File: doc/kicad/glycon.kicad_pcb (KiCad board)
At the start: 2 copper layers, 200 x 100 mm, 74 parts, among them IC2 CTC-DIP-28, J1 Arduino/system bus header, J2 PMOD USBUART conn, J3 Conn_02x24_Odd_Even, J4 Conn_01x02, J5 USB_B, Q1 IRF9540N, Q2 IRF9540N, SW1 SW_Push, SW2 SW_Push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

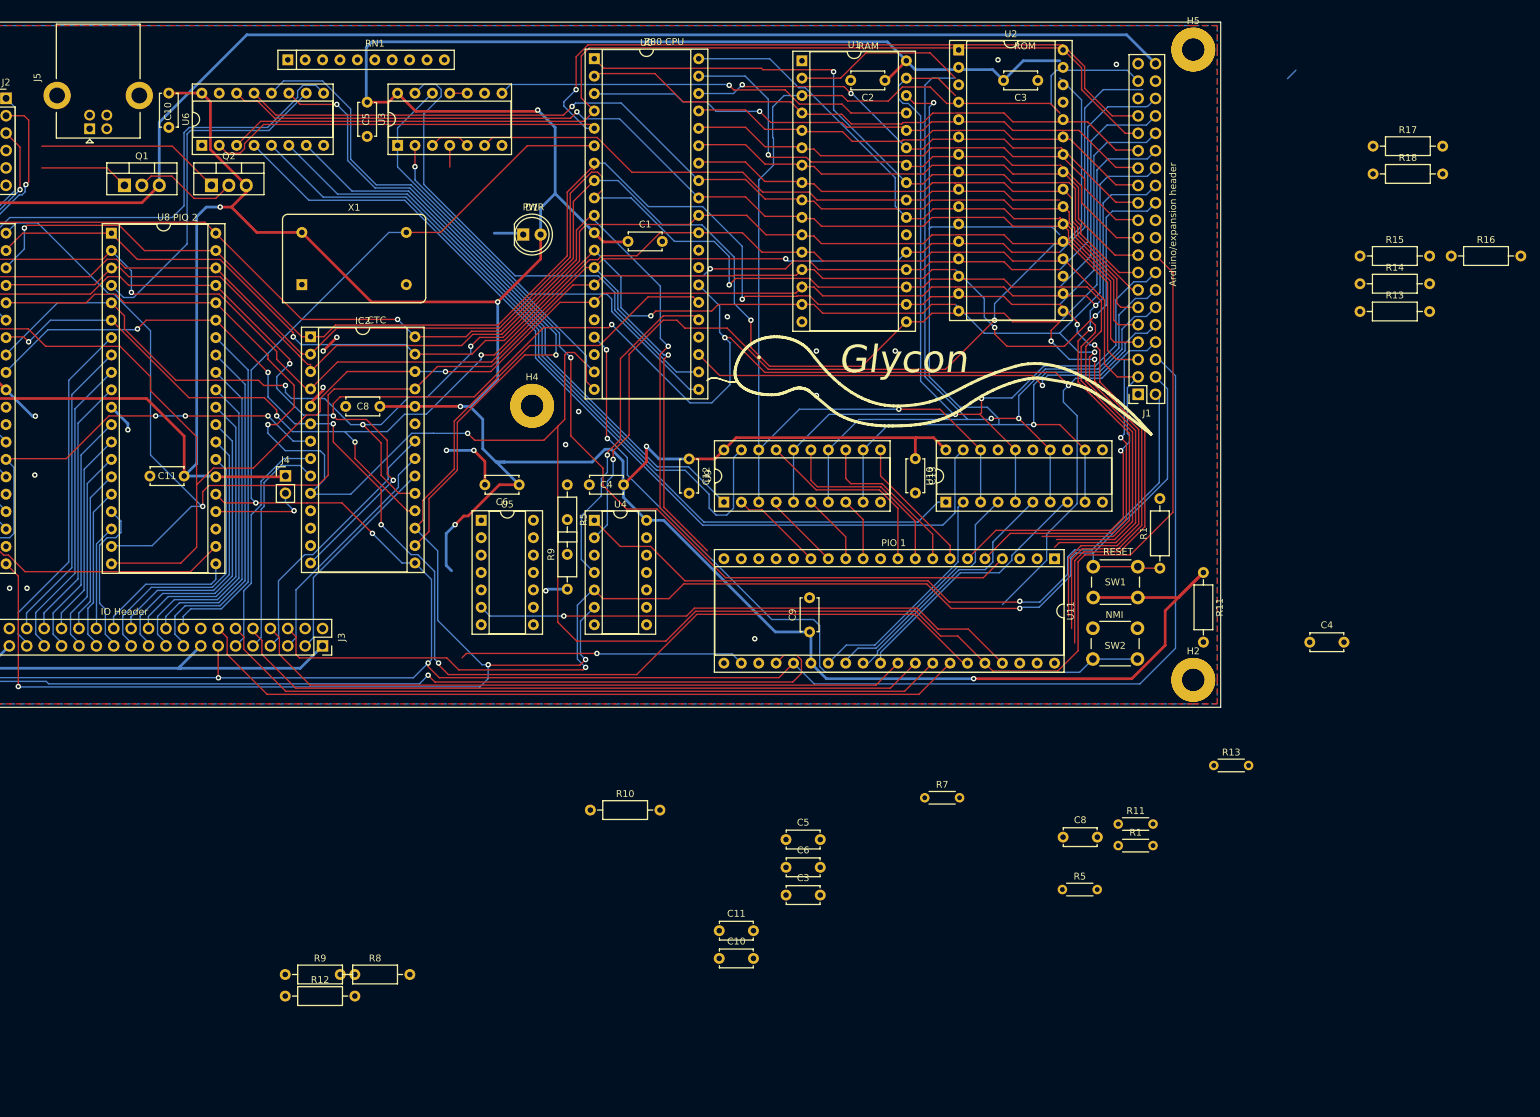
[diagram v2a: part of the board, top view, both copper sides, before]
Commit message: add resistor pack to pcb
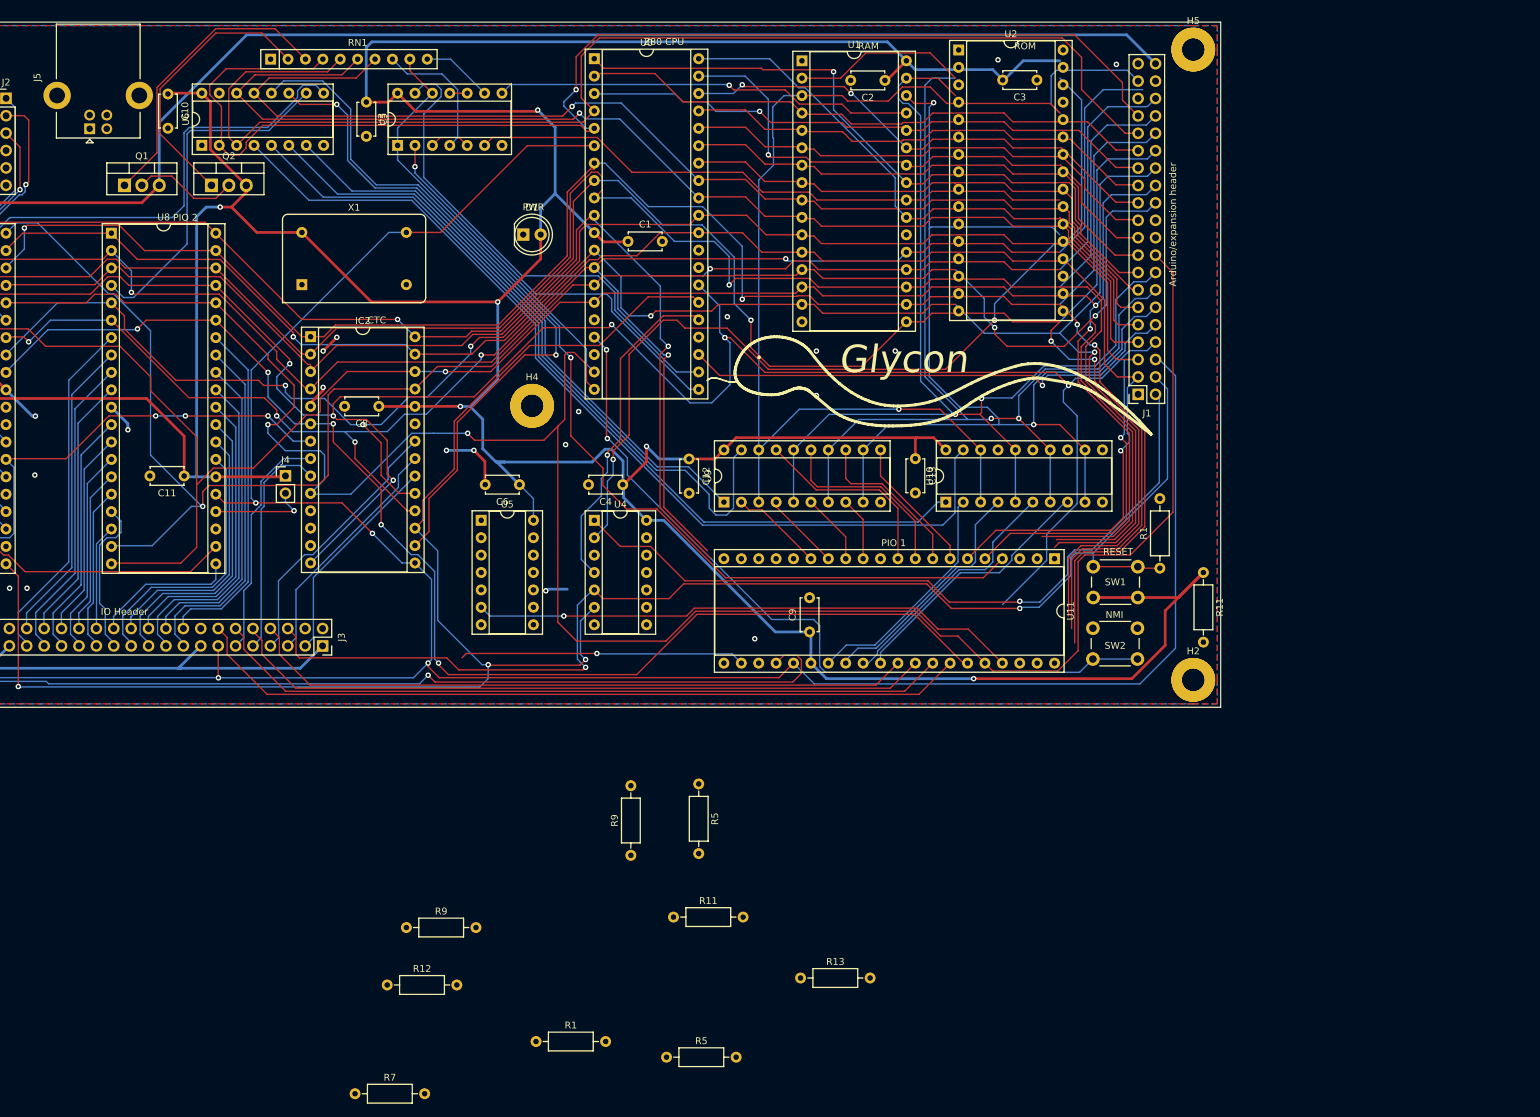
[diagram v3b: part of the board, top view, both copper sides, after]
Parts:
- removed the C10 at (70.0, 30.4)
- removed the C11 at (72.2, 86.2)
- removed the C3 at (196.8, 28.5)
- removed the C4 at (136.3, 87.5)
- removed the C5 at (98.9, 31.7)
- removed the C6 at (121.1, 87.5)
- removed the C8 at (100.8, 76.1)
- removed the C8 at (200.5, 138.9)
- removed R10, R14, R15, R16, R17, R18, R8: 10K, Resistor_THT:R_Axial_DIN0207_L6.3mm_D2.5mm_P10.16mm_Horizontal
- removed the R13 at (243.8, 62.2)
- removed the R13 at (222.5, 128.5)
- added C8: 100nF, Capacitor_THT:C_Disc_D4.7mm_W2.5mm_P5.00mm, F.Cu at (100.6, 76.1)
- added R13: 10K, Resistor_THT:R_Axial_DIN0207_L6.3mm_D2.5mm_P10.16mm_Horizontal, F.Cu at (162.2, 159.5)
- R1, R11, R5, R7: footprint Resistor_THT:R_Axial_DIN0204_L3.6mm_D1.6mm_P5.08mm_Horizontal -> Resistor_THT:R_Axial_DIN0207_L6.3mm_D2.5mm_P10.16mm_Horizontal
- moved C10 149.6 mm to (69.8, 30.5), turned to -90 degrees
- moved C3 124.5 mm to (196.7, 28.4), turned to 180 degrees
- moved C5 123.9 mm to (98.8, 31.7), turned to -90 degrees
- moved C4 102.9 mm to (136.2, 87.5), turned to 180 degrees
- moved C11 102.5 mm to (72.2, 86.2), turned to 180 degrees
- moved R7 93.7 mm to (97.2, 176.4)
- moved R1 89.7 mm to (123.6, 168.8)
- moved C6 68.1 mm to (121.2, 87.5), turned to 180 degrees
- moved R11 66.3 mm to (143.6, 150.6)
- moved R5 62.7 mm to (142.6, 171.1)
- moved R5 47.7 mm to (147.3, 131.2)
- moved R9 39.9 mm to (137.4, 141.6)
- moved R9 19.0 mm to (104.6, 152.1)
- moved R12 15.0 mm to (101.9, 160.5)
- moved RN1 2.51 mm to (84.8, 25.4)
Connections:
- net /BUSACK renamed /~{BUSACK}
- net /IEO1 renamed /IEI0
- net /IEO3 renamed /IEI2
- net Net-(U6-Pad9) renamed /~{IO_EN1}
- J1 pad 12: unconnected-(J1-Pad12) -> /A16
- J1 pad 14: unconnected-(J1-Pad14) -> /A15
- J1 pad 16: unconnected-(J1-Pad16) -> /A14
- J1 pad 37: unconnected-(J1-Pad37) -> /A14
- RN1 pad 1: Earth -> unconnected-(RN1-Pad1)
- RN1 pad 10: unconnected-(RN1-Pad10) -> /RAM WE
- RN1 pad 2: /~{IORD} -> Net-(Q2-Pad1)
- RN1 pad 3: Net-(U0-Pad22) -> Net-(Q1-Pad1)
- RN1 pad 4: /RAM/ROM OE -> /PGA1
- RN1 pad 5: Net-(RN1-Pad5) -> /PGA0
- RN1 pad 6: /A3 -> /A2
- RN1 pad 7: /A2 -> /A3
- RN1 pad 8: /PGA1 -> /RAM/ROM OE
- RN1 pad 9: /PGA0 -> Net-(RN1-Pad9)
- U0 pad 19: Net-(RN1-Pad5) -> Net-(RN1-Pad9)
- U1 pad 22: VDD -> Earth
- U3 pad 1: Net-(RN1-Pad5) -> Net-(RN1-Pad9)
- U3 pad 12: Net-(RN1-Pad5) -> Net-(RN1-Pad9)
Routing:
- net /PGA0: track 0.00 -> 180.8 mm
- net /PGA1: track 312.1 -> 189.5 mm
- net /A2: track 0.00 -> 94.2 mm, vias 0 -> 1
- net /A1: track 679.0 -> 604.4 mm, vias 7 -> 6
- net Net-(RN1-Pad9): track 0.00 -> 61.0 mm
- net Net-(RN1-Pad5): track 54.7 -> 0.00 mm
- net Net-(Q1-Pad1): track 13.1 -> 43.3 mm
- net /A3: track 148.0 -> 167.8 mm
- net /RAM/ROM OE: track 3.18 -> 20.0 mm
- net VDD: track 642.6 -> 628.9 mm, vias 7 -> 6
- net Net-(Q2-Pad1): track 27.1 -> 40.8 mm
- net /RAM WE: track 0.00 -> 10.4 mm
- net Net-(D1-Pad1): track 4.31 -> 0.28 mm
- net /D7: track 243.3 -> 241.6 mm
- net Net-(U0-Pad22): track 72.6 -> 72.0 mm
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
